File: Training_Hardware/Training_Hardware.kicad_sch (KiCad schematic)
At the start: 0 parts

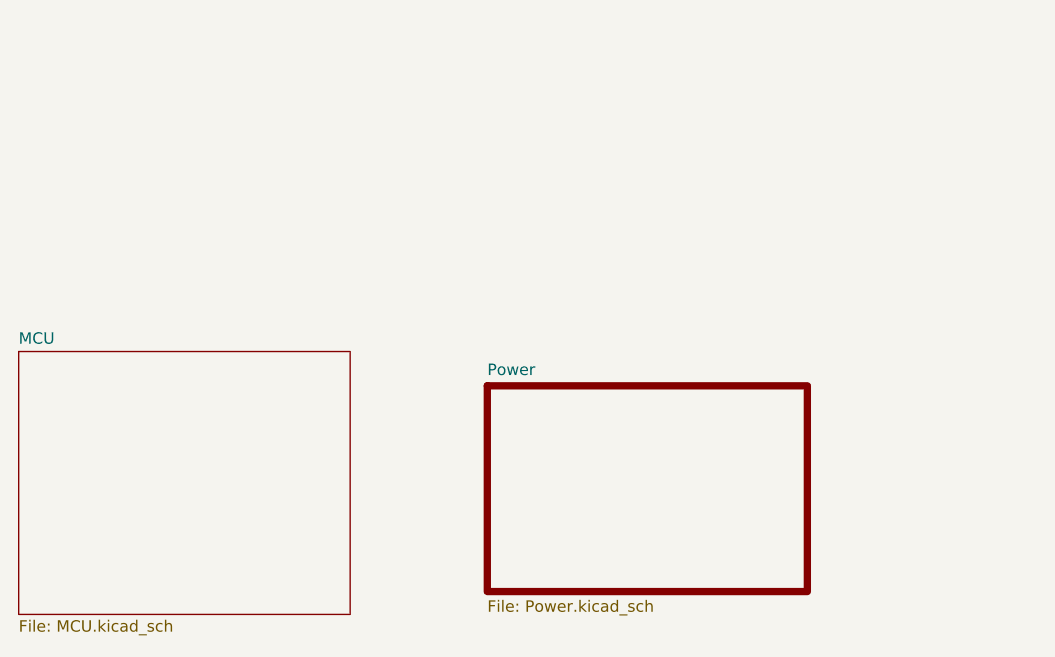
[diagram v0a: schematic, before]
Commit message: add CAN
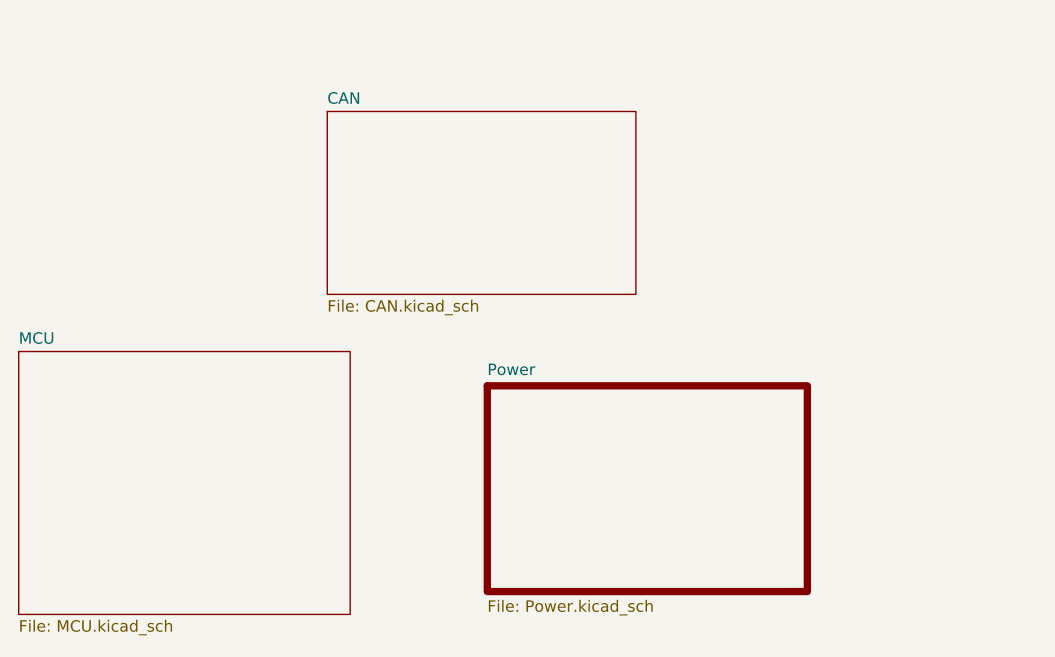
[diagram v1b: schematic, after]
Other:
- added sheet CAN (CAN.kicad_sch)
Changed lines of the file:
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@@
 	(paper "A4")
+	(sheet
+		(at 186.69 54.61)
+		(size 34.29 20.32)
+		(exclude_from_sim no)
+		(in_bom yes)
+		(on_board yes)
+		(dnp no)
+		(fields_autoplaced yes)
+		(stroke
+			(width 0.1524)
+			(type solid)
+		)
+		(fill
+			(color 0 0 0 0.0000)
+		)
+		(property "Sheetname" "CAN"
+			(at 186.69 53.8984 0)
+			(effects
+				(font
+					(size 1.27 1.27)
+				)
+				(justify left bottom)
+			)
+		)
+		(property "Sheetfile" "CAN.kicad_sch"
+			(at 186.69 75.5146 0)
+			(effects
+				(font
+					(size 1.27 1.27)
+				)
+				(justify left top)
+			)
+		)
+		(instances
+			(project "Training_Hardware"
+				(path "/11bb8091-1487-4100-afd2-5aa288c40d4f"
+					(page "4")
+				)
+			)
+		)
+	)
 	(sheet
 		(at 204.47 85.09)

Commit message: Finish Schematic
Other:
- sheet CAN ports: added RXD, STBY, TXD; removed none
- sheet MCU ports: added CRX1, CTX1, STBY; removed none
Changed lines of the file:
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@@
 	(generator_version "9.0")
 	(paper "A4")
+	(wire
+		(pts
+			(xy 220.98 64.77) (xy 228.6 64.77)
+		)
+		(stroke
+			(width 0)
+			(type default)
+		)
+	)
+	(wire
+		(pts
+			(xy 220.98 62.23) (xy 228.6 62.23)
+		)
+		(stroke
+			(width 0)
+			(type default)
+		)
+	)
+	(wire
+		(pts
+			(xy 220.98 59.69) (xy 228.6 59.69)
+		)
+		(stroke
+			(width 0)
+			(type default)
+		)
+	)
 	(sheet
 		(at 186.69 54.61)
@@
 				)
 				(justify left top)
+			)
+		)
+		(pin "RXD" output
+			(at 220.98 59.69 0)
+			(effects
+				(font
+					(size 1.27 1.27)
+				)
+				(justify right)
+			)
+		)
+		(pin "STBY" input
+			(at 220.98 62.23 0)
+			(effects
+				(font
+					(size 1.27 1.27)
+				)
+				(justify right)
+			)
+		)
+		(pin "TXD" input
+			(at 220.98 64.77 0)
+			(effects
+				(font
+					(size 1.27 1.27)
+				)
+				(justify right)
 			)
 		)
@@
 	)
 	(sheet
-		(at 152.4 81.28)
+		(at 228.6 46.99)
 		(size 36.83 29.21)
 		(exclude_from_sim no)
@@
 		)
 		(property "Sheetname" "MCU"
-			(at 152.4 80.5684 0)
+			(at 228.6 46.2784 0)
 			(effects
 				(font
@@
 		)
 		(property "Sheetfile" "MCU.kicad_sch"
-			(at 152.4 111.0746 0)
+			(at 228.6 76.7846 0)
 			(effects
 				(font
@@
 			)
 		)
+		(pin "CRX1" input
+			(at 228.6 59.69 180)
+			(effects
+				(font
+					(size 1.27 1.27)
+				)
+				(justify left)
+			)
+		)
+		(pin "CTX1" output
+			(at 228.6 64.77 180)
+			(effects
+				(font
+					(size 1.27 1.27)
+				)
+				(justify left)
+			)
+		)
+		(pin "STBY" output
+			(at 228.6 62.23 180)
+			(effects
+				(font
+					(size 1.27 1.27)
+				)
+				(justify left)
+			)
+		)
